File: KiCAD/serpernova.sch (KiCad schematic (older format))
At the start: 106 parts, among them J1 interface, Q1 2N3904, Q10 2N7000, Q2 2N3906, Q3 2N7000, Q4 2N7000, Q5 2N7000, Q6 2N7000, Q7 2N7000, Q8 2N7000, Q9 2N7000, U1 STM8S105K6B6

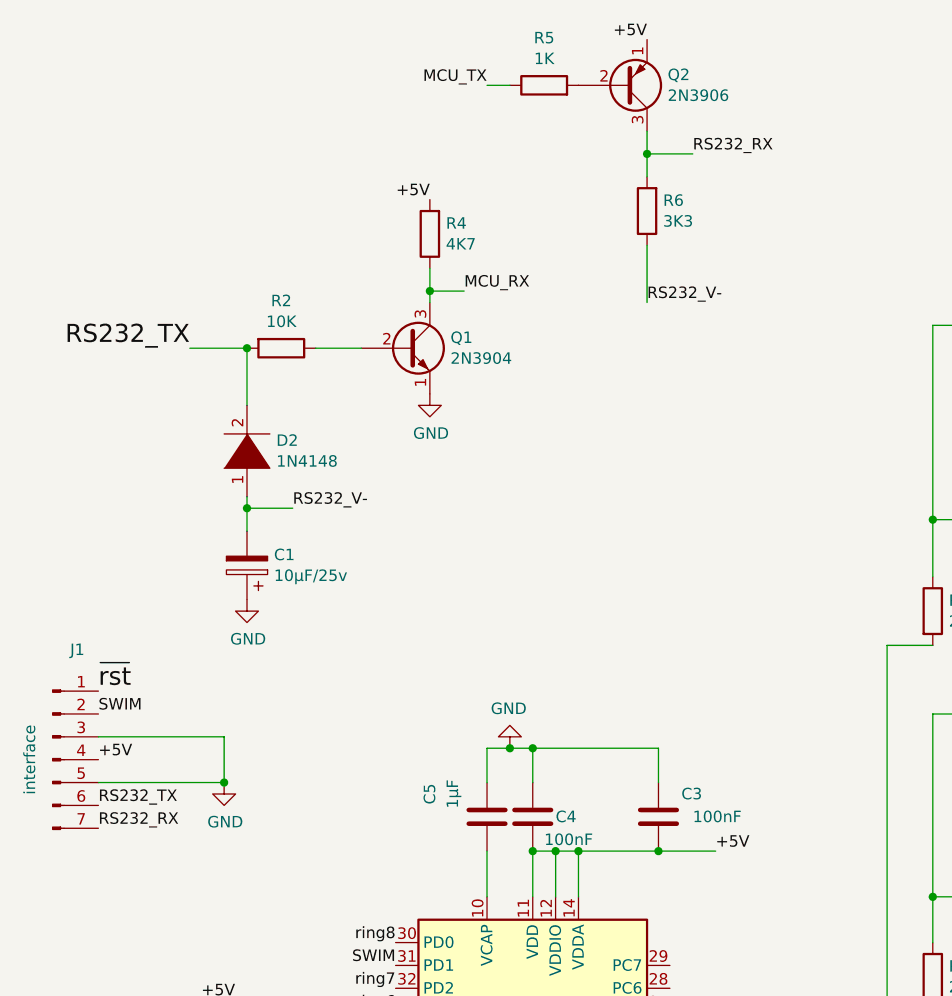
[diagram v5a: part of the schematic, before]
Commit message: Modification schématique
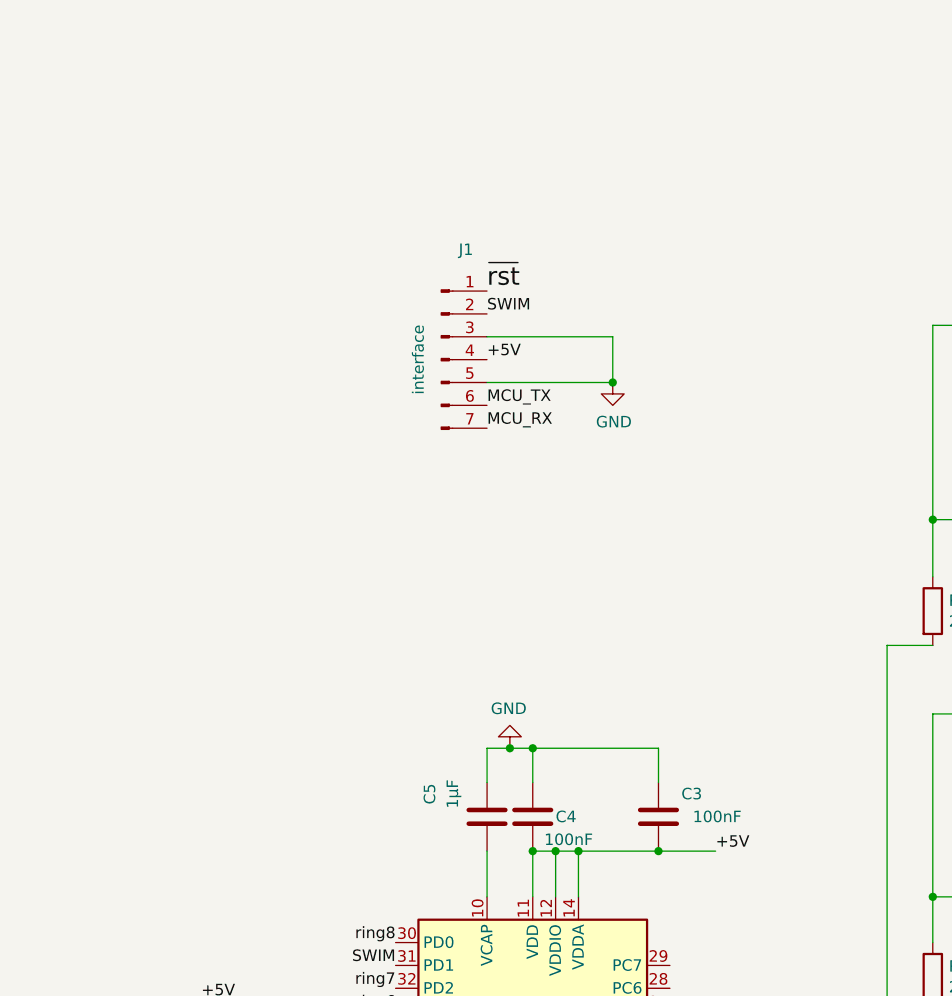
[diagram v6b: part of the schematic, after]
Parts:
- removed C1: 10µF/25v, symbol Device:CP
- removed D2: 1N4148, symbol pspice:DIODE
- removed Q1: 2N3904, Package_TO_SOT_THT:TO-92_Inline, symbol Transistor_BJT:2N3904
- removed Q2: 2N3906, Package_TO_SOT_THT:TO-92_Inline, symbol Transistor_BJT:2N3906
- removed R2: 10K, symbol Device:R
- removed R4: 4K7, symbol Device:R
- removed R5: 1K, symbol Device:R
- removed R6: 3K3, symbol Device:R
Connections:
- net RS232_RX is gone; now on net MCU_RX: J1.7 (Pin_7)
- net RS232_TX is gone; now on net MCU_TX: J1.6 (Pin_6)
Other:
- moved on the sheet: J1
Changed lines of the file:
@@
 Text Label 2350 5350 2    50   ~ 0
 MCU_TX
-$Comp
-L Transistor_BJT:2N3904 Q1
-U 1 1 5FE44A2B
-P 2400 2250
-F 0 "Q1" H 2590 2296 50  0000 L CNN
-F 1 "2N3904" H 2590 2205 50  0000 L CNN
-F 2 "Package_TO_SOT_THT:TO-92_Inline" H 2600 2175 50  0001 L CIN
-F 3 "https://www.fairchildsemi.com/datasheets/2N/2N3904.pdf" H 2400 2250 50  0001 L CNN
-	1    2400 2250
-	1    0    0    -1
-$EndComp
-$Comp
-L Transistor_BJT:2N3906 Q2
-U 1 1 5FE461F0
-P 3350 1100
-F 0 "Q2" H 3540 1054 50  0000 L CNN
-F 1 "2N3906" H 3540 1145 50  0000 L CNN
-F 2 "Package_TO_SOT_THT:TO-92_Inline" H 3550 1025 50  0001 L CIN
-F 3 "https://www.fairchildsemi.com/datasheets/2N/2N3906.pdf" H 3350 1100 50  0001 L CNN
-	1    3350 1100
-	1    0    0    1
-$EndComp
-$Comp
-L Device:R R2
-U 1 1 5FE5B695
-P 1850 2250
-F 0 "R2" V 1643 2250 50  0000 C CNN
-F 1 "10K" V 1734 2250 50  0000 C CNN
-F 2 "" V 1780 2250 50  0001 C CNN
-F 3 "~" H 1850 2250 50  0001 C CNN
-	1    1850 2250
-	0    1    1    0
-$EndComp
-$Comp
-L pspice:DIODE D2
-U 1 1 5FE5CF91
-P 1700 2700
-F 0 "D2" V 1746 2572 50  0000 R CNN
-F 1 "1N4148" V 1655 2572 50  0000 R CNN
-F 2 "" H 1700 2700 50  0001 C CNN
-F 3 "~" H 1700 2700 50  0001 C CNN
-	1    1700 2700
-	0    -1   -1   0
-$EndComp
-$Comp
-L Device:CP C1
-U 1 1 5FE5E6B7
-P 1700 3200
-F 0 "C1" H 1582 3154 50  0000 R CNN
-F 1 "10µF/25v" H 1582 3245 50  0000 R CNN
-F 2 "" H 1738 3050 50  0001 C CNN
-F 3 "~" H 1700 3200 50  0001 C CNN
-	1    1700 3200
-	-1   0    0    1
-$EndComp
-$Comp
-L power:GND #PWR01
-U 1 1 5FE5F3E3
-P 1700 3350
-F 0 "#PWR01" H 1700 3100 50  0001 C CNN
-F 1 "GND" H 1705 3177 50  0000 C CNN
-F 2 "" H 1700 3350 50  0001 C CNN
-F 3 "" H 1700 3350 50  0001 C CNN
-	1    1700 3350
-	1    0    0    -1
-$EndComp
-Wire Wire Line
-	1700 2900 1700 2950
-Wire Wire Line
-	1700 2250 1700 2500
-Wire Wire Line
-	2000 2250 2200 2250
-$Comp
-L Device:R R4
-U 1 1 5FE98402
-P 2500 1750
-F 0 "R4" H 2430 1704 50  0000 R CNN
-F 1 "4K7" H 2430 1795 50  0000 R CNN
-F 2 "" V 2430 1750 50  0001 C CNN
-F 3 "~" H 2500 1750 50  0001 C CNN
-	1    2500 1750
-	-1   0    0    1
-$EndComp
-$Comp
-L power:GND #PWR03
-U 1 1 5FEAD6AB
-P 2500 2450
-F 0 "#PWR03" H 2500 2200 50  0001 C CNN
-F 1 "GND" H 2505 2277 50  0000 C CNN
-F 2 "" H 2500 2450 50  0001 C CNN
-F 3 "" H 2500 2450 50  0001 C CNN
-	1    2500 2450
-	1    0    0    -1
-$EndComp
-Wire Wire Line
-	2500 1900 2500 2000
-Text Label 2650 2000 0    50   ~ 0
+Text Label 2750 2600 0    50   ~ 0
 MCU_RX
-Text Label 2500 1600 2    50   ~ 0
-+5V
-Wire Wire Line
-	1450 2250 1700 2250
-Connection ~ 1700 2250
-Text Label 1450 2250 2    79   ~ 0
-RS232_TX
-Text Label 1900 2950 0    50   ~ 0
-RS232_V-
-Wire Wire Line
-	1900 2950 1700 2950
-Connection ~ 1700 2950
-Wire Wire Line
-	1700 2950 1700 3050
-Wire Wire Line
-	2650 2000 2500 2000
-Connection ~ 2500 2000
-Wire Wire Line
-	2500 2000 2500 2050
-$Comp
-L Device:R R6
-U 1 1 5FF05812
-P 3450 1650
-F 0 "R6" H 3380 1604 50  0000 R CNN
-F 1 "3K3" H 3380 1695 50  0000 R CNN
-F 2 "" V 3380 1650 50  0001 C CNN
-F 3 "~" H 3450 1650 50  0001 C CNN
-	1    3450 1650
-	-1   0    0    1
-$EndComp
-Text Label 3450 2050 0    50   ~ 0
-RS232_V-
-Wire Wire Line
-	3450 1800 3450 2050
-Wire Wire Line
-	3450 1300 3450 1400
-Text Label 3650 1400 0    50   ~ 0
-RS232_RX
-Wire Wire Line
-	3650 1400 3450 1400
-Connection ~ 3450 1400
-Wire Wire Line
-	3450 1400 3450 1500
-Text Label 3450 900  2    50   ~ 0
-+5V
-$Comp
-L Device:R R5
-U 1 1 5FF46E9F
-P 3000 1100
-F 0 "R5" V 3207 1100 50  0000 C CNN
-F 1 "1K" V 3116 1100 50  0000 C CNN
-F 2 "" V 2930 1100 50  0001 C CNN
-F 3 "~" H 3000 1100 50  0001 C CNN
-	1    3000 1100
-	0    -1   -1   0
-$EndComp
-Text Label 2750 1100 2    50   ~ 0
+Text Label 2750 2500 0    50   ~ 0
 MCU_TX
-Wire Wire Line
-	2750 1100 2850 1100
 Text Notes 7200 6950 0    98   ~ 0
 SUPERNOVA \nCOPYRIGHT Jacques Deschenes, 2020
@@
 L Connector:Conn_01x07_Male J1
 U 1 1 5F84B0EE
-P 850 4050
-F 0 "J1" H 958 4531 50  0000 C CNN
-F 1 "interface" V 750 4050 50  0000 C CNN
-F 2 "" H 850 4050 50  0001 C CNN
-F 3 "~" H 850 4050 50  0001 C CNN
-	1    850  4050
+P 2550 2300
+F 0 "J1" H 2658 2781 50  0000 C CNN
+F 1 "interface" V 2450 2300 50  0000 C CNN
+F 2 "" H 2550 2300 50  0001 C CNN
+F 3 "~" H 2550 2300 50  0001 C CNN
+	1    2550 2300
 	1    0    0    -1
 $EndComp
-Text Label 1050 4050 0    50   ~ 0
+Text Label 2750 2300 0    50   ~ 0
 +5V
 $Comp
 L power:GND #PWR?
 U 1 1 5F8566E6
-P 1600 4150
-F 0 "#PWR?" H 1600 3900 50  0001 C CNN
-F 1 "GND" H 1605 3977 50  0000 C CNN
-F 2 "" H 1600 4150 50  0001 C CNN
-F 3 "" H 1600 4150 50  0001 C CNN
-	1    1600 4150
+P 3300 2400
+F 0 "#PWR?" H 3300 2150 50  0001 C CNN
+F 1 "GND" H 3305 2227 50  0000 C CNN
+F 2 "" H 3300 2400 50  0001 C CNN
+F 3 "" H 3300 2400 50  0001 C CNN
+	1    3300 2400
 	1    0    0    -1
 $EndComp
-Text Label 1050 3850 0    50   ~ 0
+Text Label 2750 2100 0    50   ~ 0
 SWIM
-Text Label 1050 3750 0    79   ~ 0
+Text Label 2750 2000 0    79   ~ 0
 ~rst
-Text Label 1050 4250 0    50   ~ 0
-RS232_TX
-Text Label 1050 4350 0    50   ~ 0
-RS232_RX
 Wire Wire Line
-	1050 4150 1600 4150
+	2750 2400 3300 2400
 Wire Wire Line
-	1600 3950 1600 4150
+	3300 2200 3300 2400
 Wire Wire Line
-	1050 3950 1600 3950
-Connection ~ 1600 4150
+	2750 2200 3300 2200
+Connection ~ 3300 2400
 Connection ~ 2850 6600
 Wire Wire Line

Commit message: mise à jour readme.md
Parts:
- renumbered C2 to C1, C5 to C2, C4 to C3, C3 to C4, D11 to D10, D12 to D11, D13 to D12, D14 to D13, D15 to D14, D16 to D15, D17 to D16, D18 to D17, D19 to D18, D20 to D19, D3 to D2, D21 to D20, D22 to D21, D23 to D22, D24 to D23, D25 to D24, D26 to D25, D27 to D26, D28 to D27, D29 to D28, D30 to D29, D4 to D3, D31 to D30, D32 to D31, D33 to D32, D34 to D33, D35 to D34, D36 to D35, D37 to D36, D38 to D37, D39 to D38, D40 to D39, D5 to D4, D41 to D40, D42 to D41, D43 to D42, D44 to D43, D45 to D44, D46 to D45, D47 to D46, D48 to D47, D49 to D48, D50 to D49, D6 to D5, D51 to D50, D52 to D51, D53 to D52, D54 to D53, D55 to D54, D56 to D55, D57 to D56, D58 to D57, D59 to D58, D60 to D59, D7 to D6, D61 to D60, D62 to D61, D63 to D62, D64 to D63, D65 to D64, D66 to D65, D8 to D7, D9 to D8, D10 to D9, Q3 to Q1, Q4 to Q2, Q5 to Q3, Q6 to Q4, Q7 to Q5, Q8 to Q6, Q9 to Q7, Q10 to Q8, R14 to R10, R15 to R11, R16 to R12, R17 to R13, R18 to R14, R19 to R15, R20 to R16, R21 to R17, R22 to R18, R3 to R2, R7 to R3, R8 to R4, R9 to R5, R10 to R6, R11 to R7, R12 to R8, R13 to R9

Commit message: montage complété mise à jour readme modification schématique ajout pullup 33K sur entrée RX
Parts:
- added R19: 33K, symbol Device:R
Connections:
- net +5V: now also R19.1
- net MCU_RX: now also R19.2
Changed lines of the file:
@@
 	3500 4450 3750 4450
 Connection ~ 3500 4450
+$Comp
+L Device:R R19
+U 1 1 5F8BA078
+P 2750 2750
+F 0 "R19" H 2680 2704 50  0000 R CNN
+F 1 "33K" H 2680 2795 50  0000 R CNN
+F 2 "" V 2680 2750 50  0001 C CNN
+F 3 "~" H 2750 2750 50  0001 C CNN
+	1    2750 2750
+	-1   0    0    1
+$EndComp
+Text Label 2750 2900 0    50   ~ 0
++5V
 $EndSCHEMATC
